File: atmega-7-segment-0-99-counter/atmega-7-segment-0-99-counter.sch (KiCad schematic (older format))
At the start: 2 parts

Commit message: Updated schematics
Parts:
- added LEFT, RIGHT: 7SEGM, symbol 7SEGM
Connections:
- net at IC?.15 ((PCINT1/OC1A)PB1): now also LEFT.10 (Segm_G), RIGHT.10 (Segm_G)
- net at IC?.23 ((PCINT8/ADC0)PC0): now also LEFT.7 (Segm_A), RIGHT.7 (Segm_A)
- net at IC?.24 ((PCINT9/ADC1)PC1): now also LEFT.6 (Segm_B), RIGHT.6 (Segm_B)
- net at IC?.25 ((PCINT10/ADC2)PC2): now also LEFT.4 (Segm_C), RIGHT.4 (Segm_C)
- net at IC?.26 ((PCINT11/ADC3)PC3): now also LEFT.2 (Segm_D), RIGHT.2 (Segm_D)
- net at IC?.27 ((PCINT12/SDA/ADC4)PC4): now also LEFT.1 (Segm_E), RIGHT.1 (Segm_E)
- net at IC?.28 ((PCINT13/SCL/ADC5)PC5): now also LEFT.9 (Segm_F), RIGHT.9 (Segm_F)
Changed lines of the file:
@@
 	4950 4900 4700 4900
 Connection ~ 4700 4900
+$Comp
+L 7SEGM LEFT
+U 1 1 57D020AC
+P 9800 2650
+F 0 "LEFT" H 9800 3300 50  0000 C CNN
+F 1 "7SEGM" H 9800 2000 50  0000 C CNN
+F 2 "" H 9800 2650 50  0000 C CNN
+F 3 "" H 9800 2650 50  0000 C CNN
+	1    9800 2650
+	1    0    0    -1
+$EndComp
+$Comp
+L 7SEGM RIGHT
+U 1 1 57D0216C
+P 9800 4100
+F 0 "RIGHT" H 9800 4750 50  0000 C CNN
+F 1 "7SEGM" H 9800 3450 50  0000 C CNN
+F 2 "" H 9800 4100 50  0000 C CNN
+F 3 "" H 9800 4100 50  0000 C CNN
+	1    9800 4100
+	1    0    0    -1
+$EndComp
+Wire Wire Line
+	6850 3450 8850 3450
+Wire Wire Line
+	8150 3450 8150 2350
+Wire Wire Line
+	8150 2350 9050 2350
+Wire Wire Line
+	6850 3550 8750 3550
+Wire Wire Line
+	8250 3550 8250 2450
+Wire Wire Line
+	8250 2450 9050 2450
+Wire Wire Line
+	6850 3650 8350 3650
+Wire Wire Line
+	8350 2550 9050 2550
+Wire Wire Line
+	6850 3750 8450 3750
+Wire Wire Line
+	8450 2650 8450 4100
+Wire Wire Line
+	8450 2650 9050 2650
+Wire Wire Line
+	6850 3850 8550 3850
+Wire Wire Line
+	8550 2750 8550 4200
+Wire Wire Line
+	8550 2750 9050 2750
+Wire Wire Line
+	6850 3950 8650 3950
+Wire Wire Line
+	8650 2850 8650 4300
+Wire Wire Line
+	8650 2850 9050 2850
+Wire Wire Line
+	8650 4300 9050 4300
+Connection ~ 8650 3950
+Wire Wire Line
+	8550 4200 9050 4200
+Connection ~ 8550 3850
+Wire Wire Line
+	8450 4100 9050 4100
+Connection ~ 8450 3750
+Wire Wire Line
+	8350 2550 8350 4000
+Wire Wire Line
+	8350 4000 9050 4000
+Connection ~ 8350 3650
+Wire Wire Line
+	8750 3550 8750 3900
+Wire Wire Line
+	8750 3900 9050 3900
+Connection ~ 8250 3550
+Wire Wire Line
+	8850 3450 8850 3800
+Wire Wire Line
+	8850 3800 9050 3800
+Connection ~ 8150 3450
+Wire Wire Line
+	7900 4400 9050 4400
+Wire Wire Line
+	6850 2700 7900 2700
+Wire Wire Line
+	7900 2700 7900 4400
+Wire Wire Line
+	9050 2950 7900 2950
+Connection ~ 7900 2950
 $EndSCHEMATC

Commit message: Progress on schematics
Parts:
- added C1, C2: 0.1uF, symbol C
- added C3, C? (x3): 3.3uF, symbol CP1
- added Q? (x2): PN2222A, symbol PN2222A
- added R1, R? (x3): 5.1k, symbol R
- added R2, R? (x3): 2.2k, symbol R
- added SW_DECREMENT, SW_DECREMENT?, SW_INCREMENT, SW_RESET_COUNTER: SW_PUSH, symbol SW_PUSH
- added U? (x5): 74HC14, symbol 74HC14
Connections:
- net GND: now also U?.2 (GND), C1.1, C2.2, C3.2, C?.2, C?.2, C?.2, Q?.1 (E), Q?.1 (E), R?.2, SW_DECREMENT.1, SW_INCREMENT.1, SW_RESET_COUNTER.1, U?.7 (GND), U?.7 (GND), U?.7 (GND), U?.7 (GND), U?.7 (GND)
- net +BATT: now reaches U?.1 (IN)
- net at U?.3 (OUT): now also IC?.20 (AVCC), IC?.21 (AREF), IC?.7 (VCC), C1.2, C2.1, R1.1, R?.1, R?.1, SW_DECREMENT?.2
- net at IC?.1 ((PCINT14/~RESET~)PC6): now also U?.2
- net at IC?.13 ((PCINT23/AIN1)PD7): now also Q?.2 (B), U?.5
- net at IC?.4 ((PCINT18/INT0)PD2): now also U?.10
- net at IC?.5 ((PCINT19/OC2B/INT1)PD3): now also U?.12
- net at IC?.6 ((PCINT20/XCK/T0)PD4): now also U?.4
- net at LEFT.8 (K): now also Q?.3 (C)
- net at RIGHT.8 (K): now also Q?.3 (C)
- new net: R1.2, R2.2, SW_RESET_COUNTER.2
- new net: C3.1, R2.1, U?.3
- new net: Q?.2 (B), U?.6
- new net: R?.2, R?.2, SW_INCREMENT.2
- new net: C?.1, R?.1, U?.11
- new net: R?.2, R?.2, SW_DECREMENT.2
- new net: C?.1, R?.1, U?.13
- new net: R?.1, R?.2
- new net: C?.1, R?.1, U?.1
- new net VCC: U?.14 (VCC), U?.14 (VCC), U?.14 (VCC), U?.14 (VCC), U?.14 (VCC)
- no-connect marks 0 -> 4
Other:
- moved on the sheet: U?

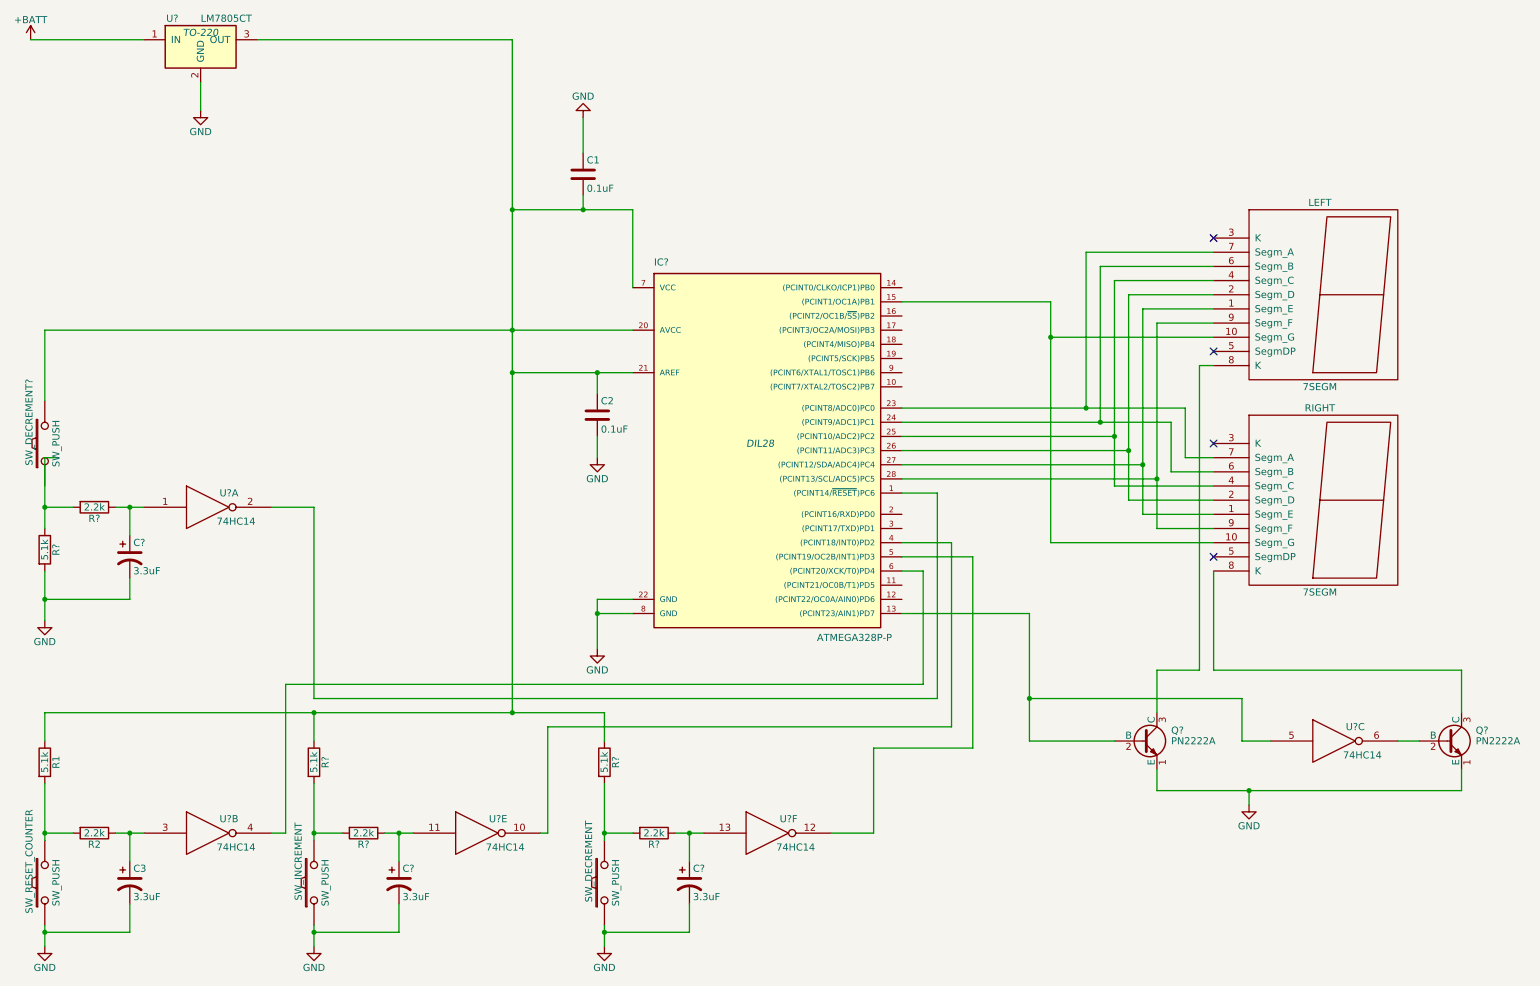
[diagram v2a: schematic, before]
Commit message: Changes to schematics
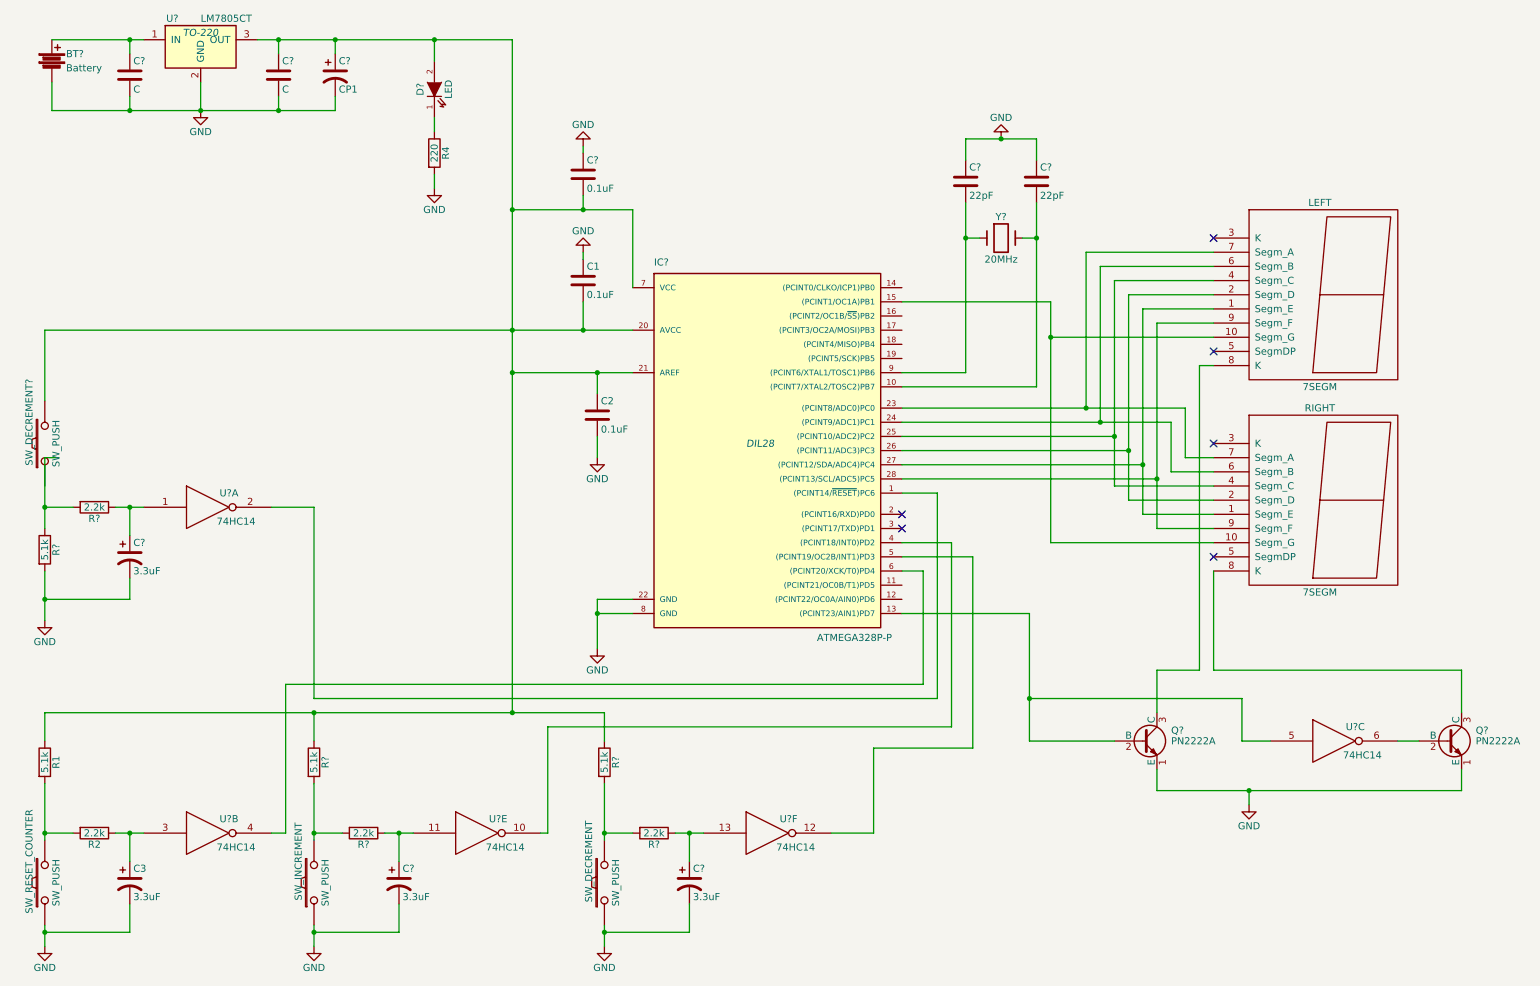
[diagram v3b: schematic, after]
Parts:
- added BT?: Battery, symbol Battery
- added C?: 0.1uF, symbol C
- added C? (x2): C, symbol C
- added C?: CP1, symbol CP1
- added C? (x2): 22pF, symbol C
- added D?: LED, symbol LED
- added R4: 220, symbol R
- added Y?: 20MHz, symbol Crystal
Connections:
- net GND: now also BT?.2, C?.1, C?.1, C?.1, C?.2, C?.2, C?.2, R4.2
- net at C1.2, C2.1, IC?.20 (AVCC)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: now also C?.1, C?.1, C?.2, D?.2 (A)
- net at IC?.10 ((PCINT7/XTAL2/TOSC2)PB7): now also C?.2, Y?.2
- net at IC?.9 ((PCINT6/XTAL1/TOSC1)PB6): now also C?.2, Y?.1
- net +BATT: no longer names the net of U?.1 (IN)
- net +BATT: now also BT?.1, C?.1
- new net: D?.1 (K), R4.1
- no-connect marks 4 -> 6
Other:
- moved on the sheet: C1
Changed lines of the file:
@@
-$EndComp
-$Comp
-L +BATT #PWR?
-U 1 1 57D02EDE
-P 700 850
-F 0 "#PWR?" H 700 700 50  0001 C CNN
-F 1 "+BATT" H 700 990 50  0000 C CNN
-F 2 "" H 700 850 50  0000 C CNN
-F 3 "" H 700 850 50  0000 C CNN
-	1    700  850
-	1    0    0    -1
 $EndComp
 $Comp
 L C C1
 U 1 1 57D03048
-P 4600 1800
-F 0 "C1" H 4625 1900 50  0000 L CNN
-F 1 "0.1uF" H 4625 1700 50  0000 L CNN
-F 2 "" H 4638 1650 50  0000 C CNN
-F 3 "" H 4600 1800 50  0000 C CNN
-	1    4600 1800
+P 4600 2550
+F 0 "C1" H 4625 2650 50  0000 L CNN
+F 1 "0.1uF" H 4625 2450 50  0000 L CNN
+F 2 "" H 4638 2400 50  0000 C CNN
+F 3 "" H 4600 2550 50  0000 C CNN
+	1    4600 2550
 	1    0    0    -1
 $EndComp
@@
 L GND #PWR?
 U 1 1 57D03160
-P 4600 1400
-F 0 "#PWR?" H 4600 1150 50  0001 C CNN
-F 1 "GND" H 4600 1250 50  0000 C CNN
-F 2 "" H 4600 1400 50  0000 C CNN
-F 3 "" H 4600 1400 50  0000 C CNN
-	1    4600 1400
+P 4600 2350
+F 0 "#PWR?" H 4600 2100 50  0001 C CNN
+F 1 "GND" H 4600 2200 50  0000 C CNN
+F 2 "" H 4600 2350 50  0000 C CNN
+F 3 "" H 4600 2350 50  0000 C CNN
+	1    4600 2350
 	-1   0    0    1
 $EndComp
@@
 Connection ~ 7900 2950
 Wire Wire Line
-	700  850  1500 850
-Wire Wire Line
 	2300 850  4100 850
 Wire Wire Line
@@
 	4700 3650 4700 3800
 Wire Wire Line
-	4600 1400 4600 1650
-Wire Wire Line
-	1900 1150 1900 1350
+	1900 1350 1900 1150
 Wire Wire Line
 	800  6100 800  6500
@@
 	9250 5800 9450 5800
 Connection ~ 7750 5500
+$Comp
+L LED D?
+U 1 1 57D0914B
+P 3550 1200
+F 0 "D?" H 3550 1300 50  0000 C CNN
+F 1 "LED" H 3550 1100 50  0000 C CNN
+F 2 "" H 3550 1200 50  0000 C CNN
+F 3 "" H 3550 1200 50  0000 C CNN
+	1    3550 1200
+	0    -1   -1   0
+$EndComp
+$Comp
+L R R4
+U 1 1 57D09216
+P 3550 1650
+F 0 "R4" V 3630 1650 50  0000 C CNN
+F 1 "220" V 3550 1650 50  0000 C CNN
+F 2 "" V 3480 1650 50  0000 C CNN
+F 3 "" H 3550 1650 50  0000 C CNN
+	1    3550 1650
+	1    0    0    -1
+$EndComp
+$Comp
+L GND #PWR?
+U 1 1 57D09293
+P 3550 1900
+F 0 "#PWR?" H 3550 1650 50  0001 C CNN
+F 1 "GND" H 3550 1750 50  0000 C CNN
+F 2 "" H 3550 1900 50  0000 C CNN
+F 3 "" H 3550 1900 50  0000 C CNN
+	1    3550 1900
+	1    0    0    -1
+$EndComp
+Wire Wire Line
+	3550 1000 3550 850
+Connection ~ 3550 850
+Wire Wire Line
+	3550 1400 3550 1500
+Wire Wire Line
+	3550 1800 3550 1900
+Wire Wire Line
+	4600 2700 4600 2900
+Connection ~ 4600 2900
+Wire Wire Line
+	4600 2350 4600 2400
+$Comp
+L C C?
+U 1 1 57D09F61
+P 4600 1800
+F 0 "C?" H 4625 1900 50  0000 L CNN
+F 1 "0.1uF" H 4625 1700 50  0000 L CNN
+F 2 "" H 4638 1650 50  0000 C CNN
+F 3 "" H 4600 1800 50  0000 C CNN
+	1    4600 1800
+	1    0    0    -1
+$EndComp
+$Comp
+L GND #PWR?
+U 1 1 57D09F67
+P 4600 1600
+F 0 "#PWR?" H 4600 1350 50  0001 C CNN
+F 1 "GND" H 4600 1450 50  0000 C CNN
+F 2 "" H 4600 1600 50  0000 C CNN
+F 3 "" H 4600 1600 50  0000 C CNN
+	1    4600 1600
+	-1   0    0    1
+$EndComp
+Wire Wire Line
+	4600 1600 4600 1650
+$Comp
+L Battery BT?
+U 1 1 57D0A107
+P 850 1000
+F 0 "BT?" H 950 1050 50  0000 L CNN
+F 1 "Battery" H 950 950 50  0000 L CNN
+F 2 "" V 850 1040 50  0000 C CNN
+F 3 "" V 850 1040 50  0000 C CNN
+	1    850  1000
+	1    0    0    -1
+$EndComp
+Wire Wire Line
+	850  850  1500 850
+Wire Wire Line
+	850  1150 850  1350
+Wire Wire Line
+	850  1350 2850 1350
+$Comp
+L C C?
+U 1 1 57D0A79D
+P 2450 1100
+F 0 "C?" H 2475 1200 50  0000 L CNN
+F 1 "C" H 2475 1000 50  0000 L CNN
+F 2 "" H 2488 950 50  0000 C CNN
+F 3 "" H 2450 1100 50  0000 C CNN
+	1    2450 1100
+	1    0    0    -1
+$EndComp
+$Comp
+L C C?
+U 1 1 57D0A826
+P 1400 1100
+F 0 "C?" H 1425 1200 50  0000 L CNN
+F 1 "C" H 1425 1000 50  0000 L CNN
+F 2 "" H 1438 950 50  0000 C CNN
+F 3 "" H 1400 1100 50  0000 C CNN
+	1    1400 1100
+	1    0    0    -1
+$EndComp
+$Comp
+L CP1 C?
+U 1 1 57D0A8FA
+P 2850 1100
+F 0 "C?" H 2875 1200 50  0000 L CNN
+F 1 "CP1" H 2875 1000 50  0000 L CNN
+F 2 "" H 2850 1100 50  0000 C CNN
+F 3 "" H 2850 1100 50  0000 C CNN
+	1    2850 1100
+	1    0    0    -1
+$EndComp
+Wire Wire Line
+	2450 950  2450 850
+Connection ~ 2450 850
+Wire Wire Line
+	2850 950  2850 850
+Connection ~ 2850 850
+Wire Wire Line
+	2850 1350 2850 1250
+Connection ~ 1900 1350
+Wire Wire Line
+	2450 1250 2450 1350
+Connection ~ 2450 1350
+Wire Wire Line
+	1400 1250 1400 1350
+Connection ~ 1400 1350
+Wire Wire Line
+	1400 950  1400 850
+Connection ~ 1400 850
+NoConn ~ 6850 4300
+NoConn ~ 6850 4200
+$Comp
+L Crystal Y?
+U 1 1 57D0B6D0
+P 7550 2250
+F 0 "Y?" H 7550 2400 50  0000 C CNN
+F 1 "20MHz" H 7550 2100 50  0000 C CNN
+F 2 "" H 7550 2250 50  0000 C CNN
+F 3 "" H 7550 2250 50  0000 C CNN
+	1    7550 2250
+	1    0    0    -1
+$EndComp
+Wire Wire Line
+	7800 3300 6850 3300
+Wire Wire Line
+	7300 3200 6850 3200
+Wire Wire Line
+	7800 2000 7800 3300
+Wire Wire Line
+	7400 2250 7300 2250
+Wire Wire Line
+	7300 2000 7300 3200
+Wire Wire Line
+	7800 2250 7700 2250
+$Comp
+L C C?
+U 1 1 57D0C106
+P 7300 1850
+F 0 "C?" H 7325 1950 50  0000 L CNN
+F 1 "22pF" H 7325 1750 50  0000 L CNN
+F 2 "" H 7338 1700 50  0000 C CNN
+F 3 "" H 7300 1850 50  0000 C CNN
+	1    7300 1850
+	1    0    0    -1
+$EndComp
+$Comp
+L C C?
+U 1 1 57D0C1AA
+P 7800 1850
+F 0 "C?" H 7825 1950 50  0000 L CNN
+F 1 "22pF" H 7825 1750 50  0000 L CNN
+F 2 "" H 7838 1700 50  0000 C CNN
+F 3 "" H 7800 1850 50  0000 C CNN
+	1    7800 1850
+	1    0    0    -1
+$EndComp
+$Comp
+L GND #PWR?
+U 1 1 57D0C23A
+P 7550 1550
+F 0 "#PWR?" H 7550 1300 50  0001 C CNN
+F 1 "GND" H 7550 1400 50  0000 C CNN
+F 2 "" H 7550 1550 50  0000 C CNN
+F 3 "" H 7550 1550 50  0000 C CNN
+	1    7550 1550
+	-1   0    0    1
+$EndComp
+Wire Wire Line
+	7300 1700 7300 1550
+Wire Wire Line
+	7800 1550 7800 1700
+Wire Wire Line
+	7300 1550 7800 1550
+Connection ~ 7550 1550
+Connection ~ 7300 2250
+Connection ~ 7800 2250
 $EndSCHEMATC

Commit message: Finished schematics + uploaded PDF version
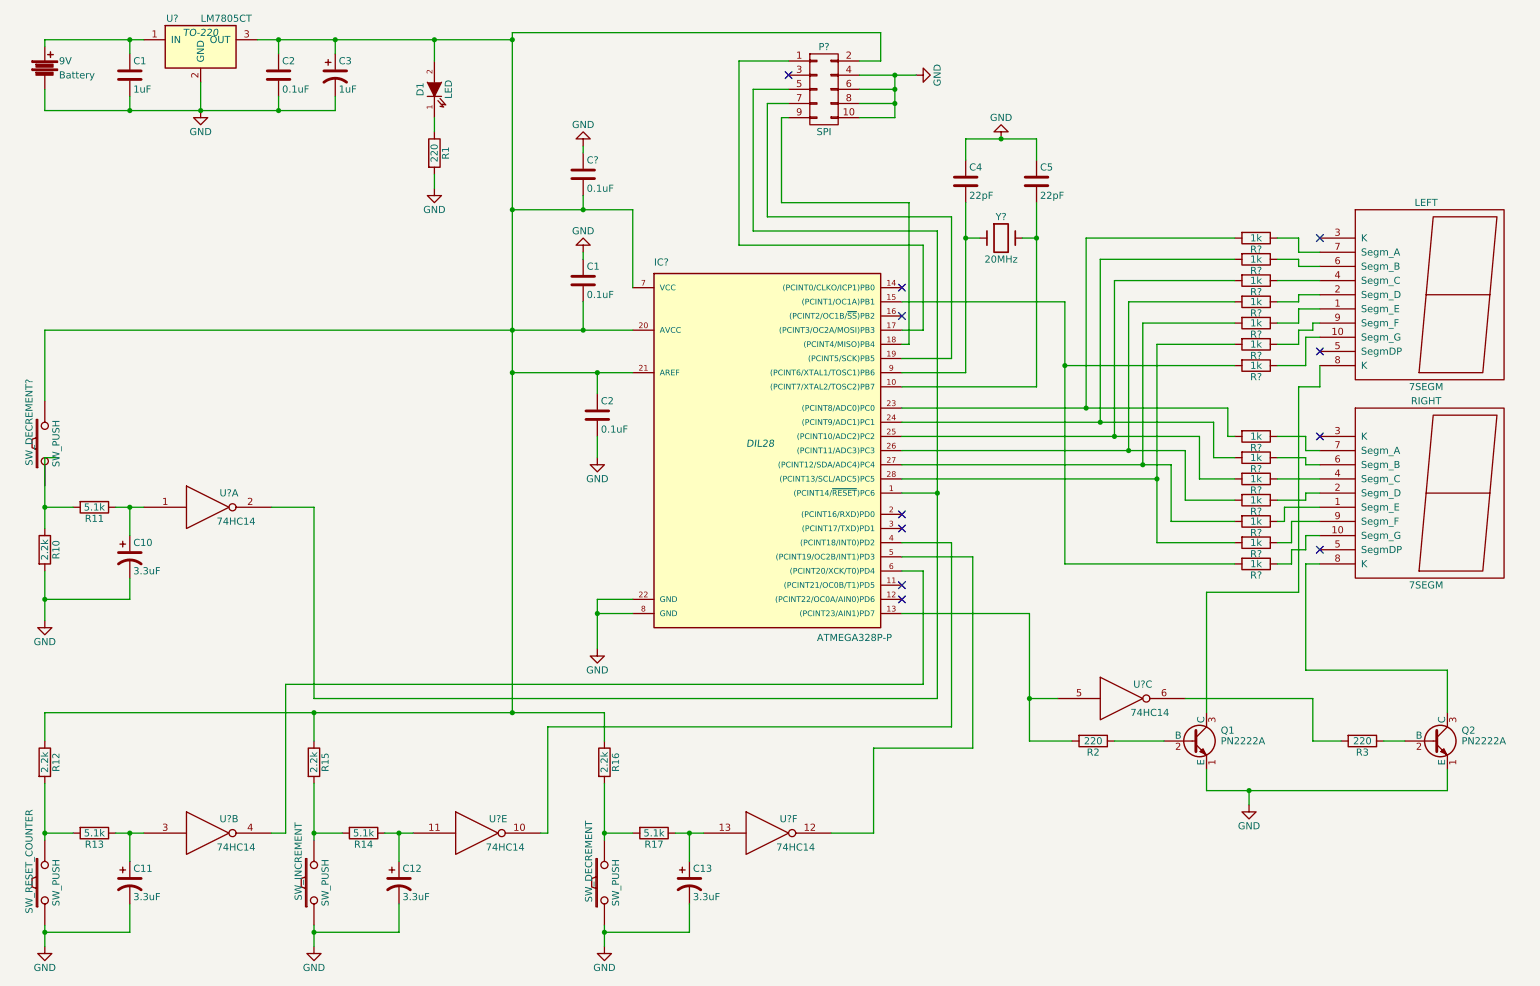
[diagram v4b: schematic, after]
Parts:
- added P?: SPI, symbol CONN_02X05
- added R2, R3: 220, symbol R
- added R? (x14): 1k, symbol R
- C1: renamed from C?; value C -> 1uF
- C2: renamed from C?; value C -> 0.1uF
- C3: renamed from C?; value CP1 -> 1uF
- R10, R15, R16: renamed from R?; value 5.1k -> 2.2k
- R11, R14, R17: renamed from R?; value 2.2k -> 5.1k
- R12: renamed from R1; value 5.1k -> 2.2k
- R13: renamed from R2; value 2.2k -> 5.1k
- gave numbers to parts that had none: 9
- renumbered C3 to C11, R4 to R1
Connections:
- net GND: now also P?.10 (P10), P?.4 (P4), P?.6 (P6), P?.8 (P8)
- net at C1.2, C2.1, C2.1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: now also P?.2 (P2)
- net at IC?.1 ((PCINT14/~RESET~)PC6), U?.2: now also P?.5 (P5)
- net at IC?.13 ((PCINT23/AIN1)PD7), U?.5: now also R2.2; no longer Q1.2 (B)
- net at IC?.17 ((PCINT3/OC2A/MOSI)PB3): now also P?.1 (P1)
- net at IC?.18 ((PCINT4/MISO)PB4): now also P?.9 (P9)
- net at IC?.19 ((PCINT5/SCK)PB5): now also P?.7 (P7)
- net at Q2.2 (B): now also R3.1; no longer U?.6
- new net: IC?.15 ((PCINT1/OC1A)PB1), R?.2, R?.2
- new net: IC?.23 ((PCINT8/ADC0)PC0), R?.2, R?.2
- new net: IC?.24 ((PCINT9/ADC1)PC1), R?.2, R?.2
- new net: IC?.25 ((PCINT10/ADC2)PC2), R?.2, R?.2
- new net: IC?.26 ((PCINT11/ADC3)PC3), R?.2, R?.2
- new net: IC?.27 ((PCINT12/SDA/ADC4)PC4), R?.2, R?.2
- new net: IC?.28 ((PCINT13/SCL/ADC5)PC5), R?.2, R?.2
- new net: LEFT.1 (Segm_E), R?.1
- new net: LEFT.10 (Segm_G), R?.1
- new net: LEFT.2 (Segm_D), R?.1
- new net: LEFT.4 (Segm_C), R?.1
- new net: LEFT.6 (Segm_B), R?.1
- new net: LEFT.7 (Segm_A), R?.1
- new net: LEFT.9 (Segm_F), R?.1
- new net: R?.1, RIGHT.1 (Segm_E)
- new net: R?.1, RIGHT.10 (Segm_G)
- new net: R?.1, RIGHT.2 (Segm_D)
- new net: R?.1, RIGHT.4 (Segm_C)
- new net: R?.1, RIGHT.6 (Segm_B)
- new net: R?.1, RIGHT.7 (Segm_A)
- new net: R?.1, RIGHT.9 (Segm_F)
- new net: Q1.2 (B), R2.1
- new net: R3.2, U?.6
- no-connect marks 6 -> 11
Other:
- moved on the sheet: 9V, LEFT, Q1, Q2, RIGHT, U?C
